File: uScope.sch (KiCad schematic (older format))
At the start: 4 parts, among them U1 K, U2 E, U3 F

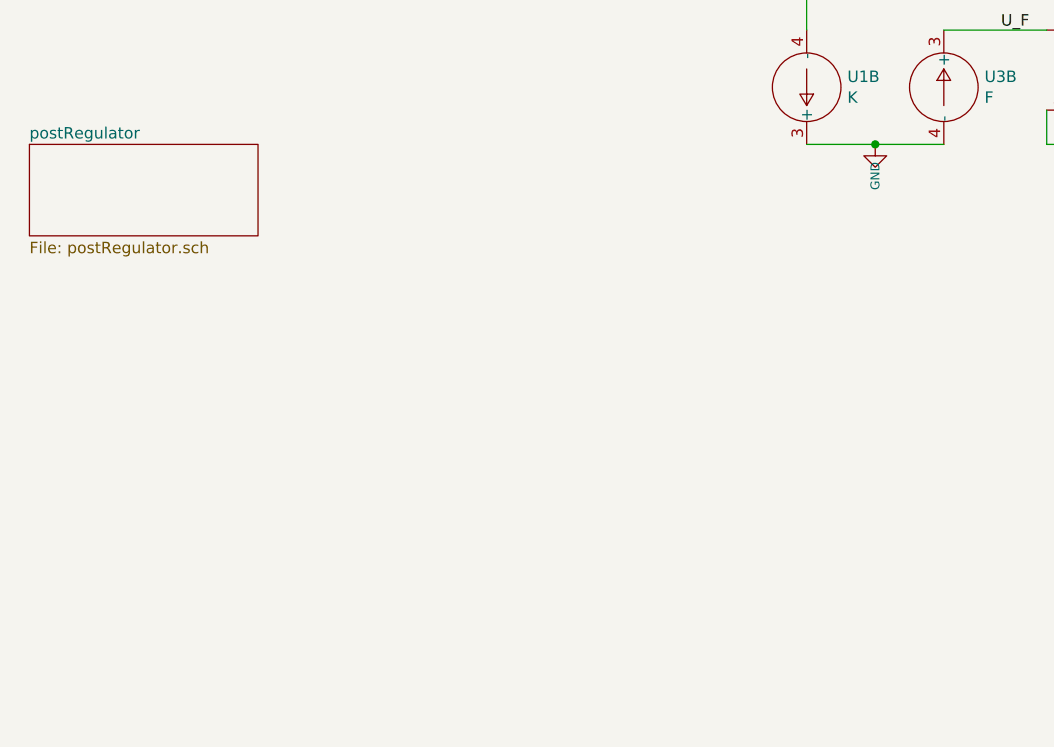
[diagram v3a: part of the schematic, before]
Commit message: - added supply sch draft
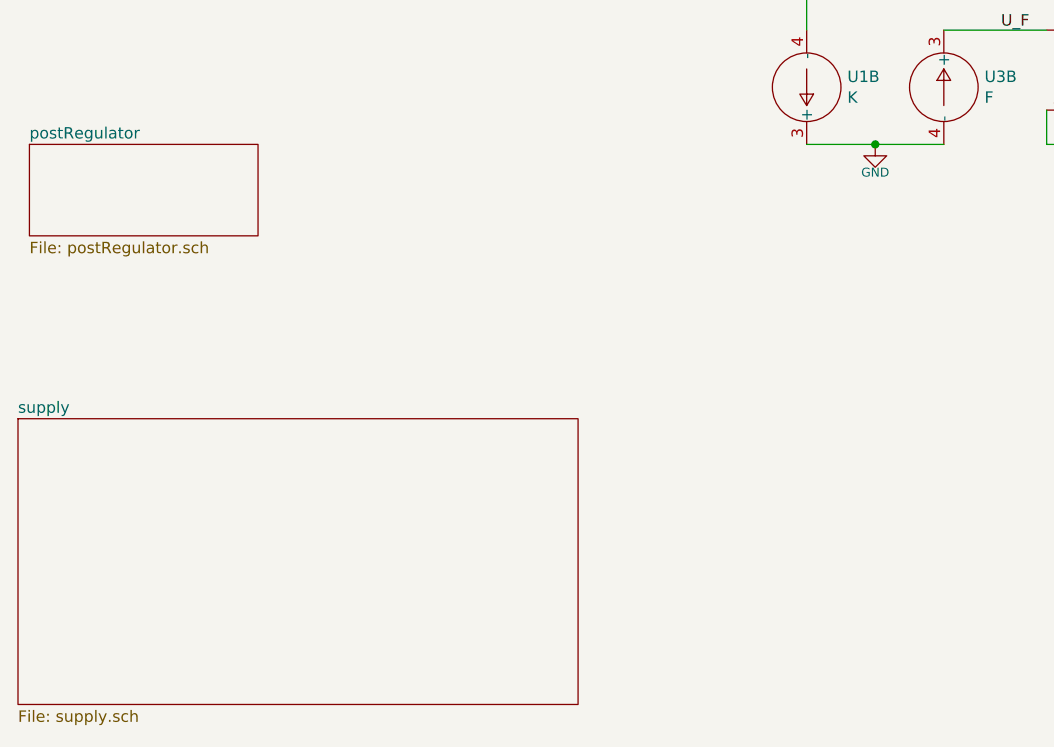
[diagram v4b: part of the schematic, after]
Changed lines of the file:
@@
 $Descr A4 11693 8268
 encoding utf-8
-Sheet 1 8
+Sheet 1 9
 Title ""
 Date ""
@@
 AR Path="/5F61B422" Ref="#PWR?"  Part="1"
 F 0 "#PWR?" H 5050 3740 50  0001 C CNN
-F 1 "GND" V 5050 3823 39  0000 R CNN
+F 1 "GND" H 5050 3800 39  0000 C TNN
 F 2 "" H 5050 3900 50  0001 C CNN
 F 3 "" H 5050 3900 50  0001 C CNN
@@
 Wire Wire Line
 	5800 3900 5800 3750
+$Sheet
+S 1300 5100 2450 1250
+U 5F620813
+F0 "supply" 50
+F1 "supply.sch" 50
+$EndSheet
 $EndSCHEMATC

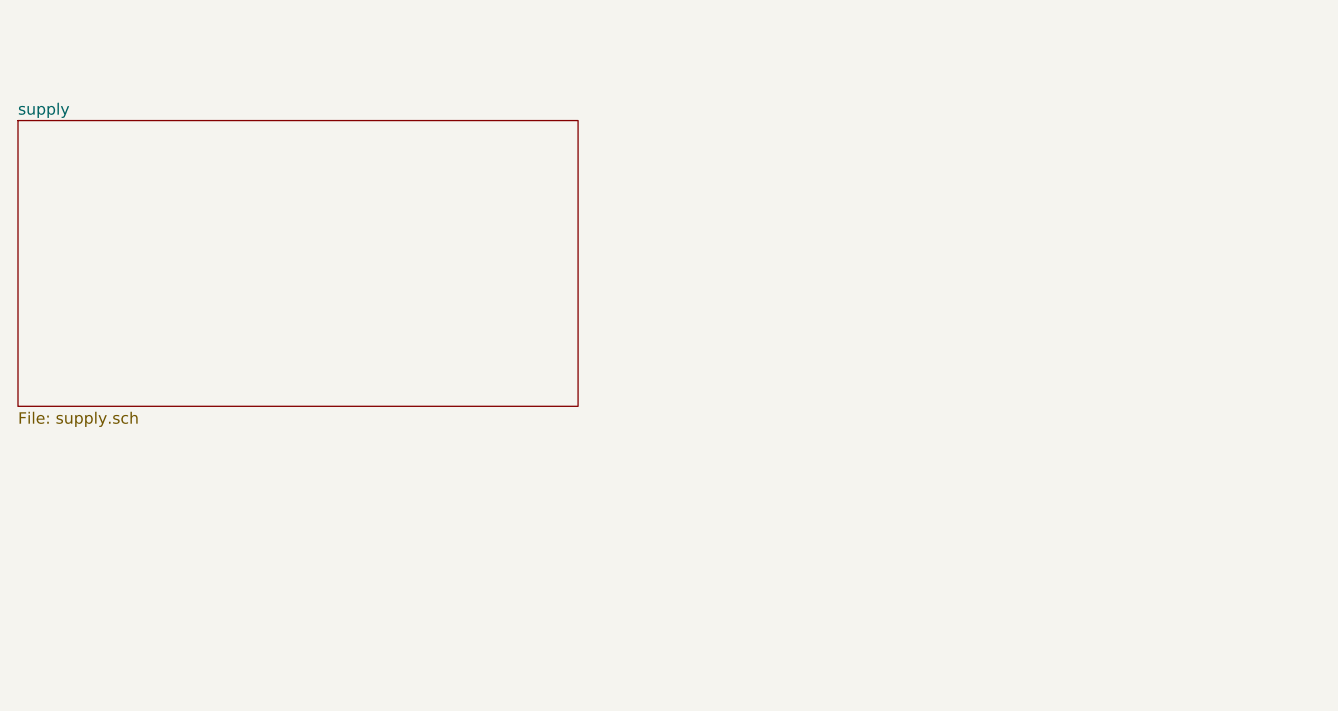
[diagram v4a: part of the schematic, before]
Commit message: - battery charger develop - added sheet (every sheet contains total number of sheets, thats beacouse here are changes in all sheets)
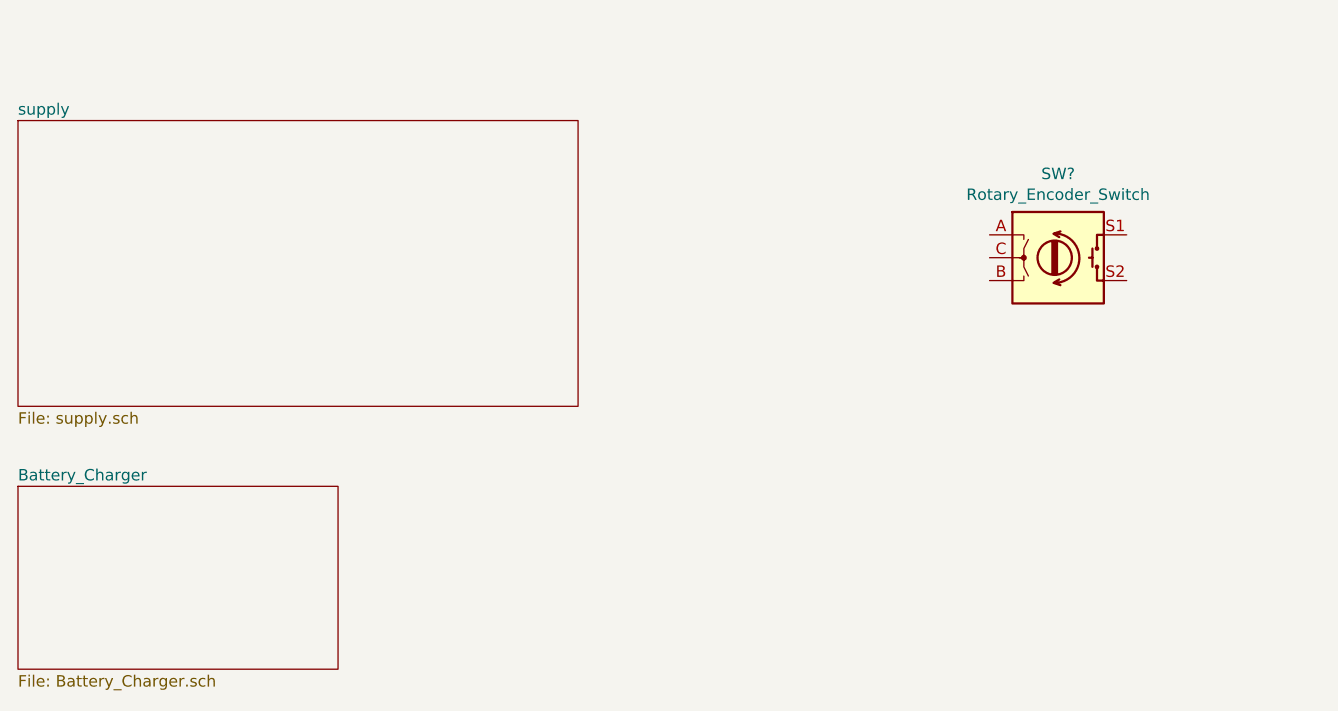
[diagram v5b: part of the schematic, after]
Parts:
- added SW?: Rotary_Encoder_Switch, symbol Device:Rotary_Encoder_Switch
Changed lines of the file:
@@
 $Descr A4 11693 8268
 encoding utf-8
-Sheet 1 9
+Sheet 1 10
 Title ""
 Date ""
@@
 F1 "supply.sch" 50
 $EndSheet
+$Comp
+L Device:Rotary_Encoder_Switch SW?
+U 1 1 5F742764
+P 5850 5700
+F 0 "SW?" H 5850 6067 50  0000 C CNN
+F 1 "Rotary_Encoder_Switch" H 5850 5976 50  0000 C CNN
+F 2 "" H 5700 5860 50  0001 C CNN
+F 3 "~" H 5850 5960 50  0001 C CNN
+	1    5850 5700
+	1    0    0    -1
+$EndComp
+$Sheet
+S 1300 6700 1400 800
+U 5F7A93EE
+F0 "Battery_Charger" 50
+F1 "Battery_Charger.sch" 50
+$EndSheet
 $EndSCHEMATC

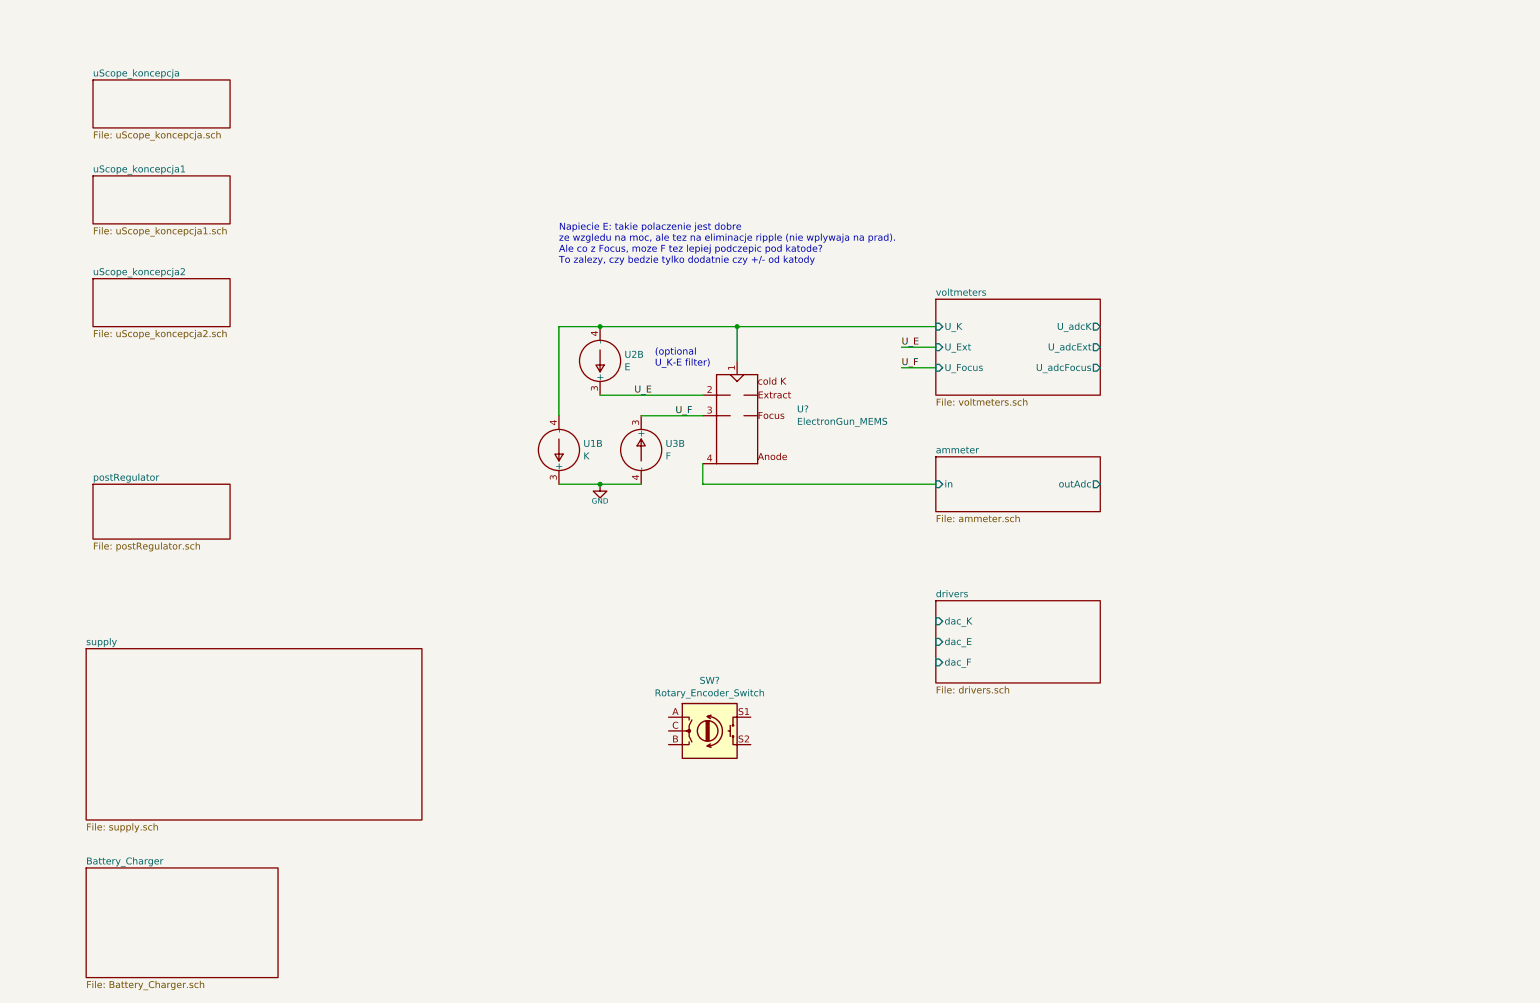
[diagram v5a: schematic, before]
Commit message: - supply converter develop - added sheet: MCU - cleanup 'koncepcja' sub-schematics
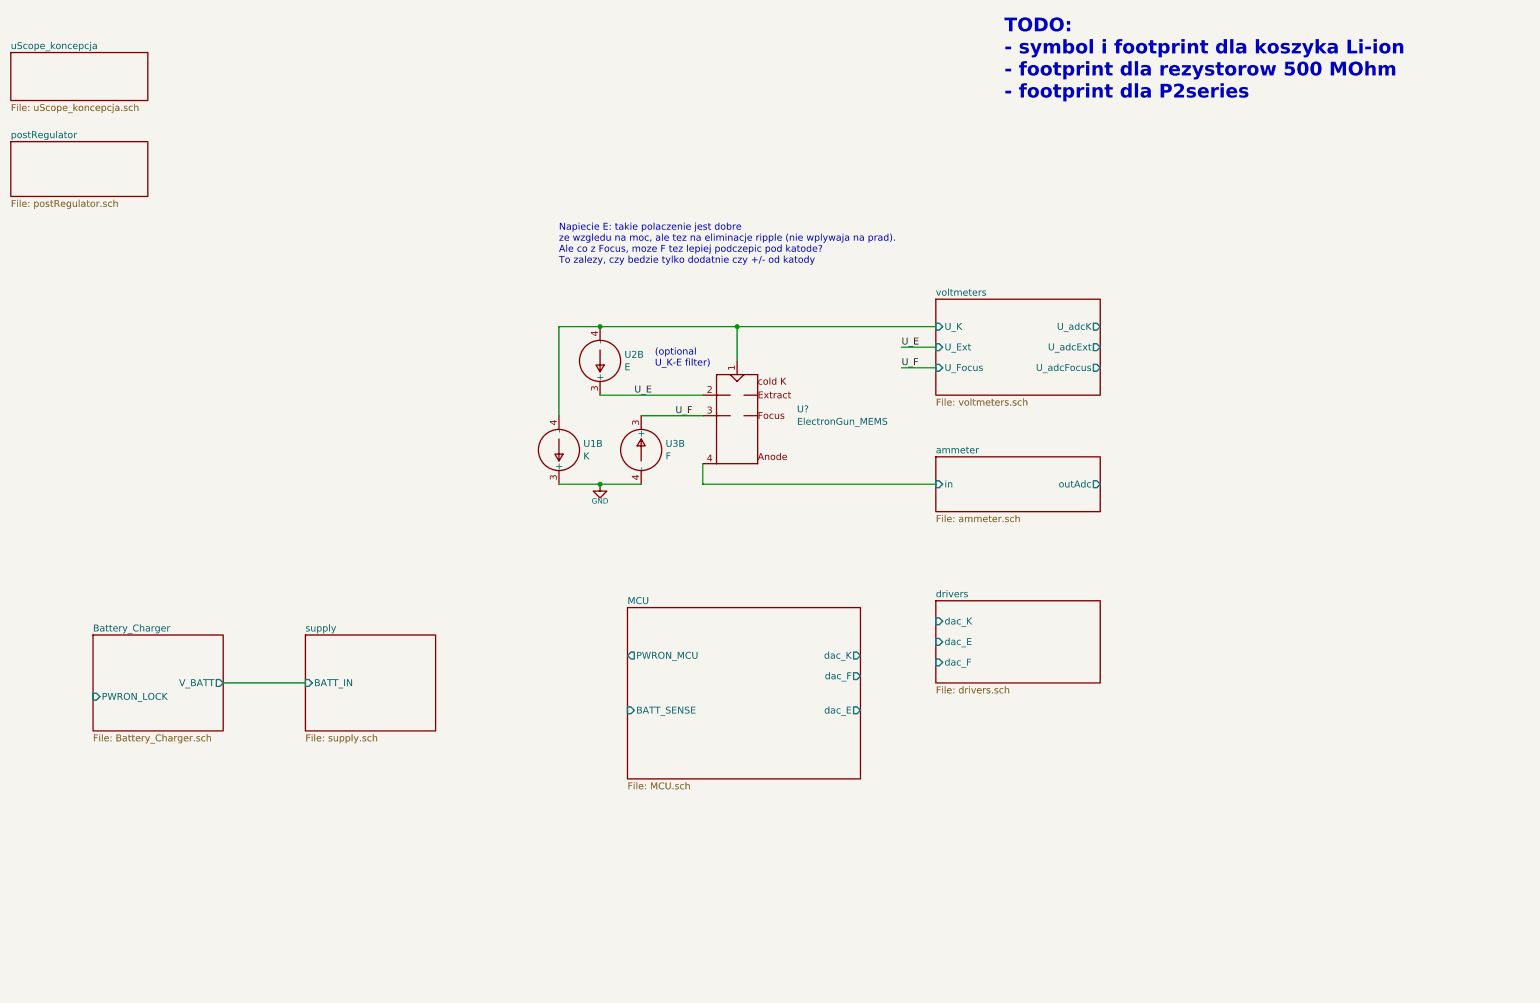
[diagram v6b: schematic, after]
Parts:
- removed SW?: Rotary_Encoder_Switch, symbol Device:Rotary_Encoder_Switch
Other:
- note added: "TODO:\n- symbol i footprint dla koszyka Li-ion\n- footprint dla rezystorow 500 MOhm\n- footprint dla P2series"
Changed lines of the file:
@@
 $Descr A4 11693 8268
 encoding utf-8
-Sheet 1 10
+Sheet 1 9
 Title ""
 Date ""
@@
 $EndDescr
 $Sheet
-S 1350 950  1000 350
+S 750  750  1000 350
 U 5F40D708
 F0 "uScope_koncepcja" 50
@@
 $EndSheet
 $Sheet
-S 1350 1650 1000 350
-U 5F40DA28
-F0 "uScope_koncepcja1" 50
-F1 "uScope_koncepcja1.sch" 50
-$EndSheet
-$Sheet
-S 1350 2400 1000 350
-U 5F40DB43
-F0 "uScope_koncepcja2" 50
-F1 "uScope_koncepcja2.sch" 50
-$EndSheet
-$Sheet
-S 1350 3900 1000 400
+S 750  1400 1000 400
 U 5F463F4C
 F0 "postRegulator" 50
@@
 	5800 3900 5800 3750
 $Sheet
-S 1300 5100 2450 1250
+S 2900 5000 950  700
 U 5F620813
 F0 "supply" 50
 F1 "supply.sch" 50
+F2 "BATT_IN" I L 2900 5350 50
 $EndSheet
-$Comp
-L Device:Rotary_Encoder_Switch SW?
-U 1 1 5F742764
-P 5850 5700
-F 0 "SW?" H 5850 6067 50  0000 C CNN
-F 1 "Rotary_Encoder_Switch" H 5850 5976 50  0000 C CNN
-F 2 "" H 5700 5860 50  0001 C CNN
-F 3 "~" H 5850 5960 50  0001 C CNN
-	1    5850 5700
-	1    0    0    -1
-$EndComp
 $Sheet
-S 1300 6700 1400 800
+S 1350 5000 950  700
 U 5F7A93EE
 F0 "Battery_Charger" 50
 F1 "Battery_Charger.sch" 50
+F2 "V_BATT" O R 2300 5350 50
+F3 "PWRON_LOCK" I L 1350 5450 50
 $EndSheet
+Wire Wire Line
+	2300 5350 2900 5350
+$Sheet
+S 5250 4800 1700 1250
+U 5F7D6767
+F0 "MCU" 50
+F1 "MCU.sch" 50
+F2 "PWRON_MCU" O L 5250 5150 50
+F3 "BATT_SENSE" I L 5250 5550 50
+F4 "dac_K" O R 6950 5150 50
+F5 "dac_F" O R 6950 5300 50
+F6 "dac_E" O R 6950 5550 50
+$EndSheet
+Text Notes 8000 1100 0    100  ~ 20
+TODO:\n- symbol i footprint dla koszyka Li-ion\n- footprint dla rezystorow 500 MOhm\n- footprint dla P2series
 $EndSCHEMATC

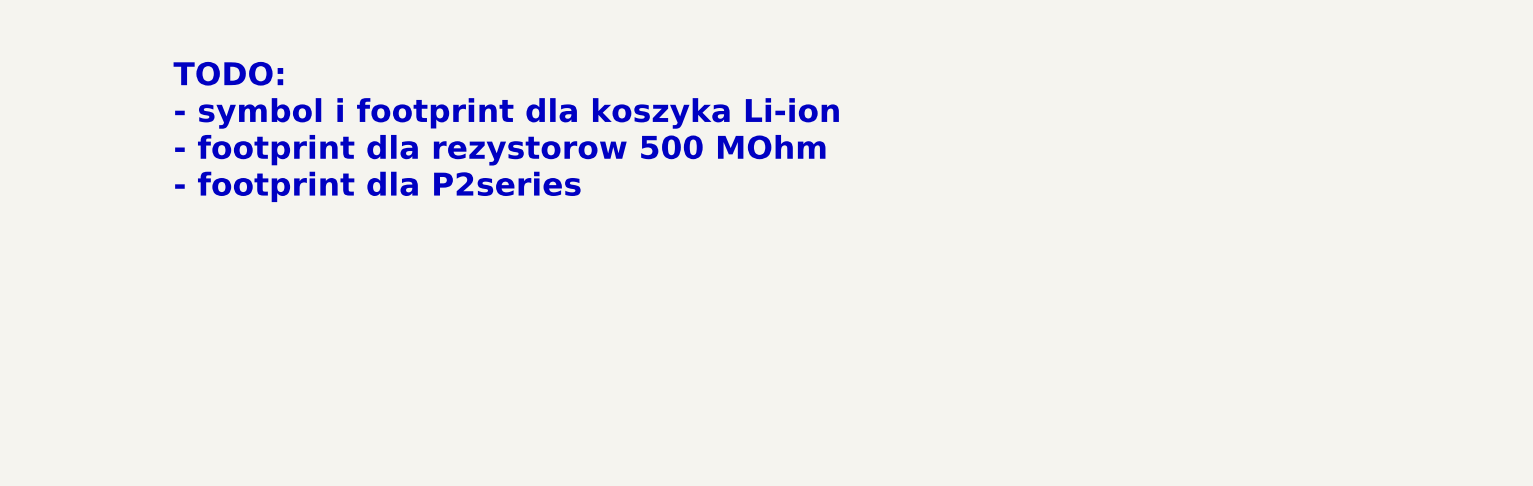
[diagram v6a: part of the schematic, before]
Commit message: - added footprint & 3D model of DC/DC HV converter - updated battery (to 2x battery holder) - some changes in supply
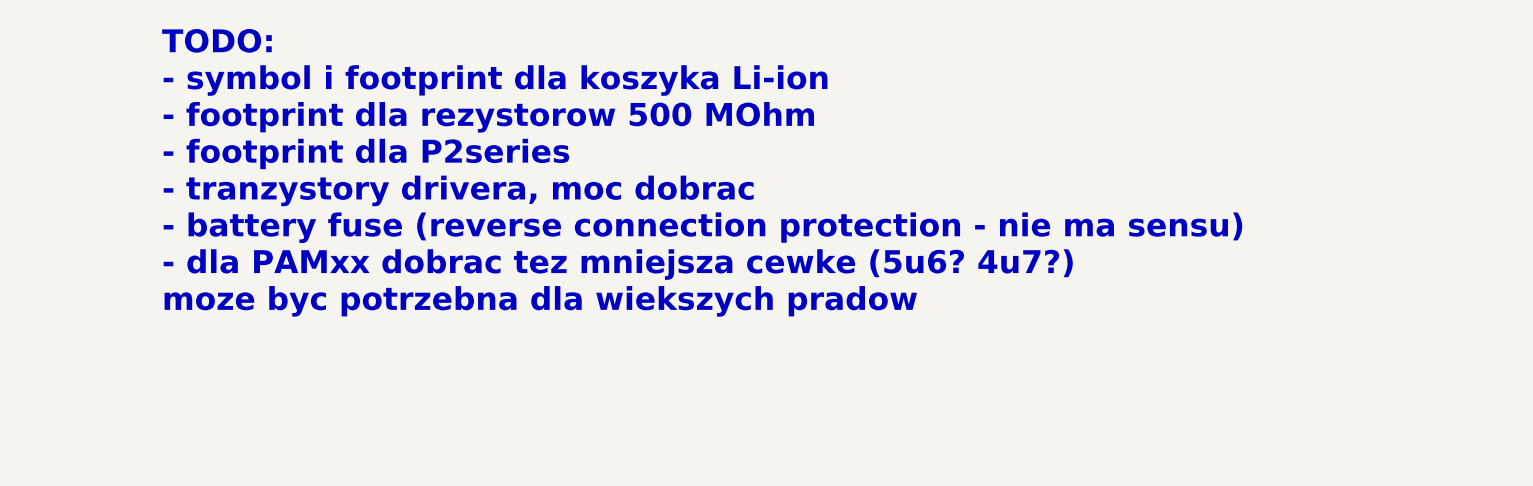
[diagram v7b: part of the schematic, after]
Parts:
- U1, U2, U3: footprint (none) -> Library_uScope:APD_P2_single
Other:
- note added: "TODO:\n- symbol i footprint dla koszyka Li-ion\n- footprint dla rezystorow 500 MOhm\n- footprint dla P2series\n- tranzystory drivera, moc dobrac\n- battery fuse (reverse connection protection - nie ma sensu)\n- dla PAMxx dobrac tez mniejsza cewke (5u6? 4u7?)\nmoze byc potrzebna dla wiekszych pradow"
- note removed: "TODO:\n- symbol i footprint dla koszyka Li-ion\n- footprint dla rezystorow 500 MOhm\n- footprint dla P2series"
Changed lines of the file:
@@
 F 0 "U1" H 4572 3604 50  0000 R CNN
 F 1 "K" H 4572 3695 50  0000 R CNN
-F 2 "" H 4750 3650 50  0001 C CNN
+F 2 "Library_uScope:APD_P2_single" H 4750 3650 50  0001 C CNN
 F 3 "" H 4750 3650 50  0001 C CNN
 	2    4750 3650
@@
 F 0 "U2" H 4872 2954 50  0000 R CNN
 F 1 "E" H 4872 3045 50  0000 R CNN
-F 2 "" H 5050 3000 50  0001 C CNN
+F 2 "Library_uScope:APD_P2_single" H 5050 3000 50  0001 C CNN
 F 3 "" H 5050 3000 50  0001 C CNN
 	2    5050 3000
@@
 F 0 "U3" H 5528 3696 50  0000 L CNN
 F 1 "F" H 5528 3605 50  0000 L CNN
-F 2 "" H 5350 3650 50  0001 C CNN
+F 2 "Library_uScope:APD_P2_single" H 5350 3650 50  0001 C CNN
 F 3 "" H 5350 3650 50  0001 C CNN
 	2    5350 3650
@@
 F6 "dac_E" O R 6950 5550 50
 $EndSheet
-Text Notes 8000 1100 0    100  ~ 20
-TODO:\n- symbol i footprint dla koszyka Li-ion\n- footprint dla rezystorow 500 MOhm\n- footprint dla P2series
+Text Notes 7950 1600 0    100  ~ 20
+TODO:\n- symbol i footprint dla koszyka Li-ion\n- footprint dla rezystorow 500 MOhm\n- footprint dla P2series\n- tranzystory drivera, moc dobrac\n- battery fuse (reverse connection protection - nie ma sensu)\n- dla PAMxx dobrac tez mniejsza cewke (5u6? 4u7?)\nmoze byc potrzebna dla wiekszych pradow
 $EndSCHEMATC

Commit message: - changes..
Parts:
- added C? (x2): 10n, Capacitor_moja:C_Disc_D18.0_W5.0_P10.0mm, symbol Device:C_Small
- added R? (x2): VR25 470k, Resistor_THT:R_Axial_DIN0207_L6.3mm_D2.5mm_P10.16mm_Horizontal, symbol Device:R
- added U?: RHV2-1212S/R20, symbol power_my:RECOM_RHV2_single_vert
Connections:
- net labels added: +12V, -VDC, HV+12V, HVGND
- wire segments 14 -> 20
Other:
- note added: "TODO:\n- tranzystory drivera, moc dobrac\n- battery fuse (reverse connection protection - nie ma sensu)\n- dla PAMxx dobrac tez mniejsza cewke (5u6? 4u7?)\nmoze byc potrzebna dla wiekszych pradow\n- ! polaczenie zrodel zasilania moze byc uwarunkowane tym, z ktorej strony wplywa prad. Bo nie sa to zrodla push-pull, tylko push."
- note removed: "TODO:\n- symbol i footprint dla koszyka Li-ion\n- footprint dla rezystorow 500 MOhm\n- footprint dla P2series\n- tranzystory drivera, moc dobrac\n- battery fuse (reverse connection protection - nie ma sensu)\n- dla PAMxx dobrac tez mniejsza cewke (5u6? 4u7?)\nmoze byc potrzebna dla wiekszych pradow"
- moved on the sheet: U1B, U3B
